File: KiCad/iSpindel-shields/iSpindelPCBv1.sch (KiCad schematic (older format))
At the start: 9 parts, among them SW1 SW_DPDT_x2, U1 GY-521, U2 LoRa_Ra-02, U3 WeMos_mini, U4 TP4056-shield-6PIN, U5 DS18B20

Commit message: adjust switch and charger
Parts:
- removed SW1: SW_DPDT_x2, KiCadCustomLibs:SK12D07VG3, symbol SW_DPDT_x2
- added SW1: SW_SPDT, KiCadCustomLibs:SK12D07VG3, symbol SW_SPDT
- added SW2: SW_SPDT, KiCadCustomLibs:SS-12F23, symbol SW_SPDT
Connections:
- net +5V: now also SW1.2 (B), SW2.2 (B)
- net at U4.3 (OUT+): now also SW1.1 (A), SW2.1 (A)
- no-connect marks 15 -> 16
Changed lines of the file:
@@
 $EndComp
 $Comp
-L GND #PWR01
+L GND #PWR4
 U 1 1 5B524582
 P 3250 3600
-F 0 "#PWR01" H 3250 3350 50  0001 C CNN
+F 0 "#PWR4" H 3250 3350 50  0001 C CNN
 F 1 "GND" H 3250 3450 50  0000 C CNN
 F 2 "" H 3250 3600 50  0001 C CNN
@@
 $EndComp
 $Comp
-L +5V #PWR02
+L +5V #PWR8
 U 1 1 5B524B0C
 P 4650 2850
-F 0 "#PWR02" H 4650 2700 50  0001 C CNN
+F 0 "#PWR8" H 4650 2700 50  0001 C CNN
 F 1 "+5V" H 4650 2990 50  0000 C CNN
 F 2 "" H 4650 2850 50  0001 C CNN
@@
 	4850 2850 4650 2850
 $Comp
-L GND #PWR03
+L GND #PWR7
 U 1 1 5B524D7B
 P 4350 2950
-F 0 "#PWR03" H 4350 2700 50  0001 C CNN
+F 0 "#PWR7" H 4350 2700 50  0001 C CNN
 F 1 "GND" H 4350 2800 50  0000 C CNN
 F 2 "" H 4350 2950 50  0001 C CNN
@@
 	5850 3450 5850 3850
 $Comp
-L +5V #PWR04
+L +5V #PWR11
 U 1 1 5B530550
 P 6150 3800
-F 0 "#PWR04" H 6150 3650 50  0001 C CNN
+F 0 "#PWR11" H 6150 3650 50  0001 C CNN
 F 1 "+5V" H 6150 3940 50  0000 C CNN
 F 2 "" H 6150 3800 50  0001 C CNN
@@
 $EndComp
 $Comp
-L GND #PWR05
+L GND #PWR14
 U 1 1 5B530B26
 P 7250 3450
-F 0 "#PWR05" H 7250 3200 50  0001 C CNN
+F 0 "#PWR14" H 7250 3200 50  0001 C CNN
 F 1 "GND" H 7250 3300 50  0000 C CNN
 F 2 "" H 7250 3450 50  0001 C CNN
 F 3 "" H 7250 3450 50  0001 C CNN
 	1    7250 3450
-	1    0    0    -1
-$EndComp
-$Comp
-L SW_DPDT_x2 SW1
-U 1 1 5B533766
-P 7150 4700
-F 0 "SW1" H 7150 4870 50  0000 C CNN
-F 1 "SW_DPDT_x2" H 7150 4500 50  0000 C CNN
-F 2 "KiCadCustomLibs:SK12D07VG3" H 7150 4700 50  0001 C CNN
-F 3 "" H 7150 4700 50  0001 C CNN
-	1    7150 4700
 	1    0    0    -1
 $EndComp
@@
 $EndComp
 $Comp
-L +5V #PWR06
+L +5V #PWR12
 U 1 1 5B53007F
 P 6700 4700
-F 0 "#PWR06" H 6700 4550 50  0001 C CNN
+F 0 "#PWR12" H 6700 4550 50  0001 C CNN
 F 1 "+5V" H 6700 4840 50  0000 C CNN
 F 2 "" H 6700 4700 50  0001 C CNN
@@
 $EndComp
 $Comp
-L +5V #PWR07
+L +5V #PWR13
 U 1 1 5B5300A5
 P 7250 2850
-F 0 "#PWR07" H 7250 2700 50  0001 C CNN
+F 0 "#PWR13" H 7250 2700 50  0001 C CNN
 F 1 "+5V" H 7250 2990 50  0000 C CNN
 F 2 "" H 7250 2850 50  0001 C CNN
@@
 $EndComp
 $Comp
-L +5V #PWR08
+L +5V #PWR3
 U 1 1 5B5300CB
 P 3250 2400
-F 0 "#PWR08" H 3250 2250 50  0001 C CNN
+F 0 "#PWR3" H 3250 2250 50  0001 C CNN
 F 1 "+5V" H 3250 2540 50  0000 C CNN
 F 2 "" H 3250 2400 50  0001 C CNN
@@
 	7350 4450 7350 4600
 $Comp
-L GND #PWR09
+L GND #PWR9
 U 1 1 5B5307B4
 P 4900 4950
-F 0 "#PWR09" H 4900 4700 50  0001 C CNN
+F 0 "#PWR9" H 4900 4700 50  0001 C CNN
 F 1 "GND" H 4900 4800 50  0000 C CNN
 F 2 "" H 4900 4950 50  0001 C CNN
@@
 $EndComp
 $Comp
-L GND #PWR010
+L GND #PWR1
 U 1 1 5B5351DB
 P 2450 4250
-F 0 "#PWR010" H 2450 4000 50  0001 C CNN
+F 0 "#PWR1" H 2450 4000 50  0001 C CNN
 F 1 "GND" H 2450 4100 50  0000 C CNN
 F 2 "" H 2450 4250 50  0001 C CNN
@@
 Connection ~ 2450 4250
 $Comp
-L +3.3V #PWR011
+L +3.3V #PWR10
 U 1 1 5B53531D
 P 6100 2850
-F 0 "#PWR011" H 6100 2700 50  0001 C CNN
+F 0 "#PWR10" H 6100 2700 50  0001 C CNN
 F 1 "+3.3V" H 6100 2990 50  0000 C CNN
 F 2 "" H 6100 2850 50  0001 C CNN
@@
 Connection ~ 6100 2850
 $Comp
-L +3.3V #PWR012
+L +3.3V #PWR2
 U 1 1 5B53535F
 P 2650 4100
-F 0 "#PWR012" H 2650 3950 50  0001 C CNN
+F 0 "#PWR2" H 2650 3950 50  0001 C CNN
 F 1 "+3.3V" H 2650 4240 50  0000 C CNN
 F 2 "" H 2650 4100 50  0001 C CNN
@@
 	3750 4150 4100 4150
 $Comp
-L GND #PWR013
+L GND #PWR6
 U 1 1 5B5366A9
 P 4100 4150
-F 0 "#PWR013" H 4100 3900 50  0001 C CNN
+F 0 "#PWR6" H 4100 3900 50  0001 C CNN
 F 1 "GND" H 4100 4000 50  0000 C CNN
 F 2 "" H 4100 4150 50  0001 C CNN
@@
 NoConn ~ 4850 3250
 $Comp
-L GND #PWR014
+L GND #PWR5
 U 1 1 5B54D258
 P 3750 4850
-F 0 "#PWR014" H 3750 4600 50  0001 C CNN
+F 0 "#PWR5" H 3750 4600 50  0001 C CNN
 F 1 "GND" H 3750 4700 50  0000 C CNN
 F 2 "" H 3750 4850 50  0001 C CNN
@@
 	1    0    0    -1
 $EndComp
+NoConn ~ 7350 5350
+Wire Wire Line
+	6950 5250 6700 5250
+Wire Wire Line
+	6700 5250 6700 4700
+Connection ~ 6700 4700
+Connection ~ 7350 4600
+Wire Wire Line
+	7350 4600 7500 4600
+Wire Wire Line
+	7500 4600 7500 5150
+Wire Wire Line
+	7500 5150 7350 5150
+$Comp
+L SW_SPDT SW2
+U 1 1 5B570A3C
+P 7150 5250
+F 0 "SW2" H 7150 5420 50  0000 C CNN
+F 1 "SW_SPDT" H 7150 5050 50  0000 C CNN
+F 2 "KiCadCustomLibs:SS-12F23" H 7150 5250 50  0001 C CNN
+F 3 "" H 7150 5250 50  0001 C CNN
+	1    7150 5250
+	1    0    0    -1
+$EndComp
+$Comp
+L SW_SPDT SW1
+U 1 1 5B570AC9
+P 7150 4700
+F 0 "SW1" H 7150 4870 50  0000 C CNN
+F 1 "SW_SPDT" H 7150 4500 50  0000 C CNN
+F 2 "KiCadCustomLibs:SK12D07VG3" H 7150 4700 50  0001 C CNN
+F 3 "" H 7150 4700 50  0001 C CNN
+	1    7150 4700
+	1    0    0    -1
+$EndComp

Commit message: Add TH variant
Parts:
- D1: footprint Diodes_SMD:D_SOD-123 -> Resistors_Universal:Resistor_SMD+THTuniversal_0805to1206_RM10_HandSoldering
- R1, R2: footprint Resistors_SMD:R_0603 -> Resistors_Universal:Resistor_SMD+THTuniversal_0805to1206_RM10_HandSoldering
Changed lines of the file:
@@
 F 0 "R2" V 6930 3000 50  0000 C CNN
 F 1 "4.7k" V 6850 3000 50  0000 C CNN
-F 2 "Resistors_SMD:R_0603" V 6780 3000 50  0001 C CNN
+F 2 "Resistors_Universal:Resistor_SMD+THTuniversal_0805to1206_RM10_HandSoldering" V 6780 3000 50  0001 C CNN
 F 3 "" H 6850 3000 50  0001 C CNN
 	1    6850 3000
@@
 F 0 "R1" V 6080 3850 50  0000 C CNN
 F 1 "220K" V 6000 3850 50  0000 C CNN
-F 2 "Resistors_SMD:R_0603" V 5930 3850 50  0001 C CNN
+F 2 "Resistors_Universal:Resistor_SMD+THTuniversal_0805to1206_RM10_HandSoldering" V 5930 3850 50  0001 C CNN
 F 3 "" H 6000 3850 50  0001 C CNN
 	1    6000 3850
 	0    -1   -1   0
 $EndComp
-Wire Wire Line
-	5850 3450 5850 3850
 $Comp
 L +5V #PWR11
@@
 F 0 "D1" H 6250 3450 50  0000 C CNN
 F 1 "Schottky" H 6200 3250 50  0000 C CNN
-F 2 "Diodes_SMD:D_SOD-123" H 6250 3350 50  0001 C CNN
+F 2 "Resistors_Universal:Resistor_SMD+THTuniversal_0805to1206_RM10_HandSoldering" H 6250 3350 50  0001 C CNN
 F 3 "" H 6250 3350 50  0001 C CNN
 	1    6250 3350
@@
 Text Label 6100 2950 2    60   ~ 0
 NSS
-Wire Wire Line
-	6150 3800 6150 3850
 Wire Wire Line
 	2750 4450 2550 4450
@@
 	1    0    0    -1
 $EndComp
+Wire Wire Line
+	6150 3800 6150 3850
+Wire Wire Line
+	5850 3450 5850 3850
 $EndSCHEMATC

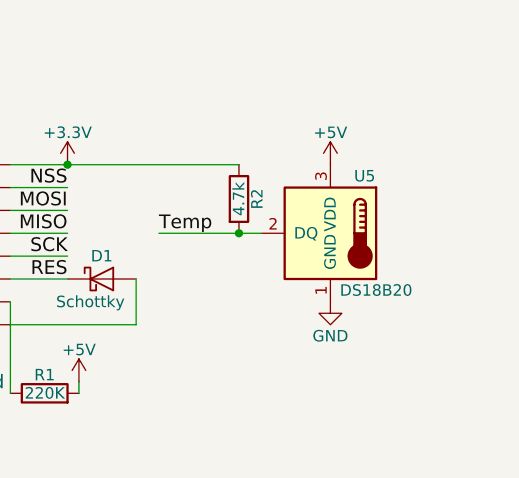
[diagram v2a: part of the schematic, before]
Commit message: Some minor adjustments to PCB. Added capacitor to DS
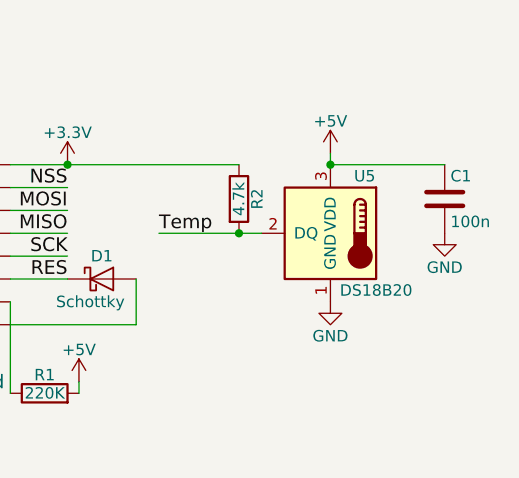
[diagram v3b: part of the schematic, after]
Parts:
- added C1: 100n, Capacitors_SMD:C_0805_HandSoldering, symbol C
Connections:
- net +5V: now also C1.1
- net GND: now also C1.2
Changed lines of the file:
@@
 L +5V #PWR13
 U 1 1 5B5300A5
-P 7250 2850
-F 0 "#PWR13" H 7250 2700 50  0001 C CNN
-F 1 "+5V" H 7250 2990 50  0000 C CNN
-F 2 "" H 7250 2850 50  0001 C CNN
-F 3 "" H 7250 2850 50  0001 C CNN
-	1    7250 2850
+P 7250 2800
+F 0 "#PWR13" H 7250 2650 50  0001 C CNN
+F 1 "+5V" H 7250 2940 50  0000 C CNN
+F 2 "" H 7250 2800 50  0001 C CNN
+F 3 "" H 7250 2800 50  0001 C CNN
+	1    7250 2800
 	1    0    0    -1
 $EndComp
@@
 Wire Wire Line
 	5850 3450 5850 3850
+Wire Wire Line
+	7250 2850 7250 2800
+$Comp
+L C C1
+U 1 1 5B740F13
+P 7750 3000
+F 0 "C1" H 7775 3100 50  0000 L CNN
+F 1 "100n" H 7775 2900 50  0000 L CNN
+F 2 "Capacitors_SMD:C_0805_HandSoldering" H 7788 2850 50  0001 C CNN
+F 3 "" H 7750 3000 50  0001 C CNN
+	1    7750 3000
+	1    0    0    -1
+$EndComp
+$Comp
+L GND #PWR15
+U 1 1 5B740F67
+P 7750 3150
+F 0 "#PWR15" H 7750 2900 50  0001 C CNN
+F 1 "GND" H 7750 3000 50  0000 C CNN
+F 2 "" H 7750 3150 50  0001 C CNN
+F 3 "" H 7750 3150 50  0001 C CNN
+	1    7750 3150
+	1    0    0    -1
+$EndComp
+Wire Wire Line
+	7750 2850 7250 2850
+Connection ~ 7250 2850
 $EndSCHEMATC
